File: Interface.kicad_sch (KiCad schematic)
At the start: 12 parts

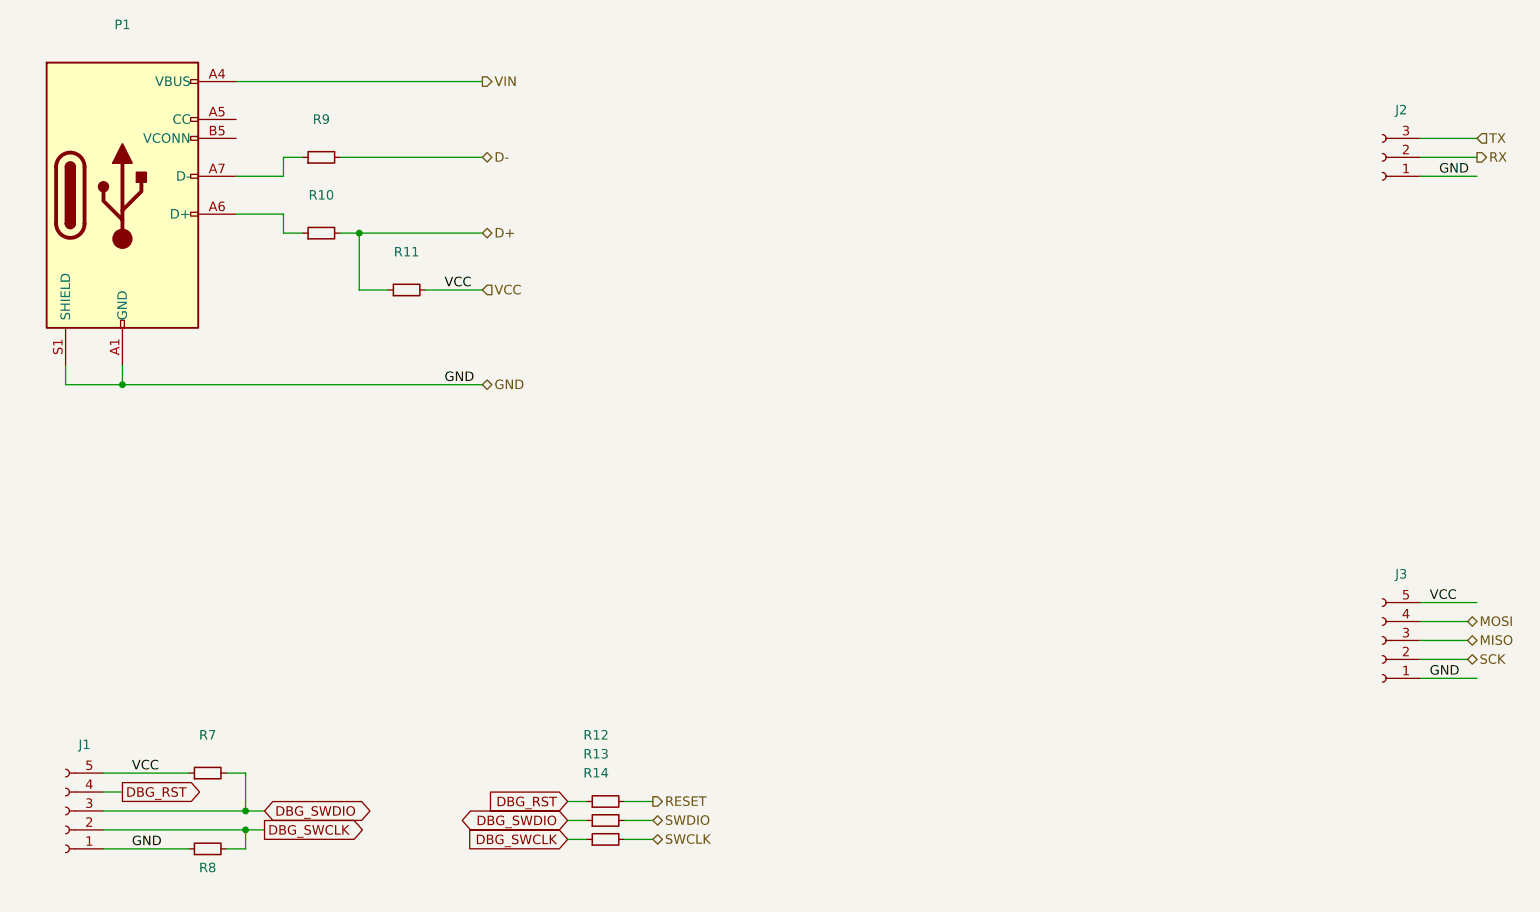
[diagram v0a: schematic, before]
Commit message: update goose60 sch footprint
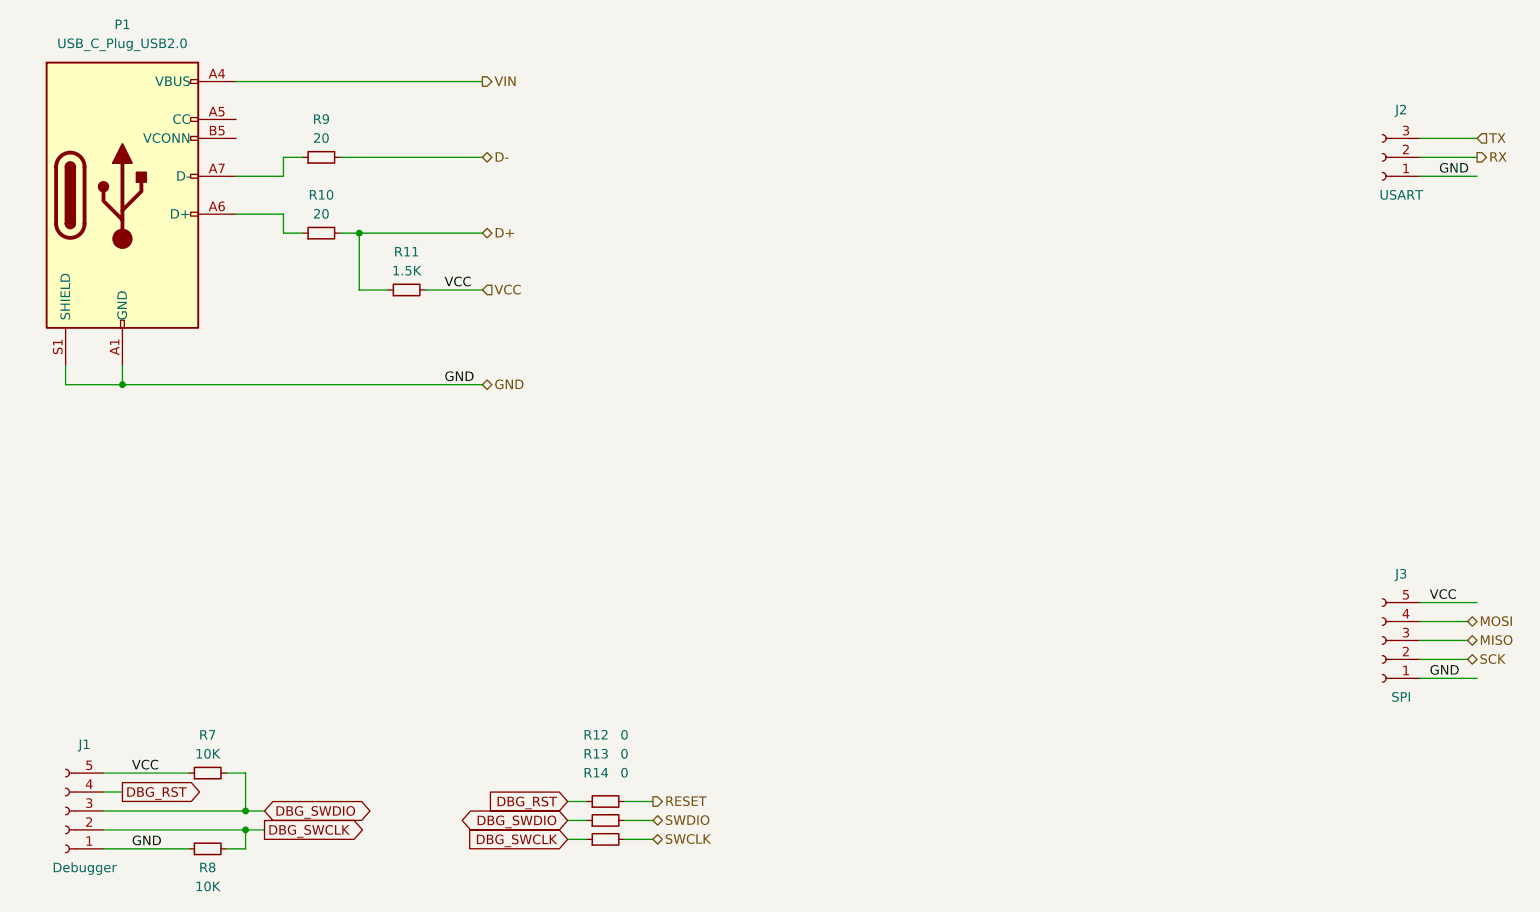
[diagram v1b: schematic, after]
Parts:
- J1: value (none) -> Debugger; footprint (none) -> Connector_PinHeader_2.00mm:PinHeader_1x05_P2.00mm_Vertical
- J2: value (none) -> USART; footprint (none) -> Connector_PinHeader_2.00mm:PinHeader_1x03_P2.00mm_Vertical
- J3: value (none) -> SPI; footprint (none) -> Connector_PinHeader_2.00mm:PinHeader_1x05_P2.00mm_Vertical
- P1: value (none) -> USB_C_Plug_USB2.0; footprint (none) -> Connector_USB:USB_C_Receptacle_HRO_TYPE-C-31-M-12
- R10, R9: value (none) -> 20; footprint (none) -> Resistor_SMD:R_0805_2012Metric
- R11: value (none) -> 1.5K; footprint (none) -> Resistor_SMD:R_0805_2012Metric
- R12, R13, R14: value (none) -> 0; footprint (none) -> Resistor_SMD:R_0805_2012Metric
- R7, R8: value (none) -> 10K; footprint (none) -> Resistor_SMD:R_0805_2012Metric
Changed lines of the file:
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@@
     (in_bom yes) (on_board yes)
     (property "Reference" "R11" (id 0) (at 93.98 60.96 90))
-    (property "Value" "" (id 1) (at 93.98 63.5 90))
-    (property "Footprint" "" (id 2) (at 93.98 66.04 0)
+    (property "Value" "1.5K" (id 1) (at 93.98 63.5 90))
+    (property "Footprint" "Resistor_SMD:R_0805_2012Metric" (id 2) (at 93.98 66.04 0)
       (effects (font (size 1.27 1.27)) hide)
     )
@@
     (in_bom yes) (on_board yes)
     (property "Reference" "R8" (id 0) (at 67.31 143.51 90))
-    (property "Value" "" (id 1) (at 67.31 146.05 90))
-    (property "Footprint" "" (id 2) (at 67.31 140.97 0)
+    (property "Value" "10K" (id 1) (at 67.31 146.05 90))
+    (property "Footprint" "Resistor_SMD:R_0805_2012Metric" (id 2) (at 67.31 140.97 0)
       (effects (font (size 1.27 1.27)) hide)
     )
@@
     (in_bom yes) (on_board yes)
     (property "Reference" "R14" (id 0) (at 119.38 130.81 90))
-    (property "Value" "" (id 1) (at 123.19 130.81 90))
-    (property "Footprint" "" (id 2) (at 120.65 139.7 0)
+    (property "Value" "0" (id 1) (at 123.19 130.81 90))
+    (property "Footprint" "Resistor_SMD:R_0805_2012Metric" (id 2) (at 120.65 139.7 0)
       (effects (font (size 1.27 1.27)) hide)
     )
@@
     (in_bom yes) (on_board yes)
     (property "Reference" "J3" (id 0) (at 227.33 104.14 0))
-    (property "Value" "" (id 1) (at 227.33 120.65 0))
-    (property "Footprint" "" (id 2) (at 224.79 113.03 0)
+    (property "Value" "SPI" (id 1) (at 227.33 120.65 0))
+    (property "Footprint" "Connector_PinHeader_2.00mm:PinHeader_1x05_P2.00mm_Vertical" (id 2) (at 224.79 113.03 0)
       (effects (font (size 1.27 1.27)) hide)
     )
@@
     (in_bom yes) (on_board yes) (fields_autoplaced)
     (property "Reference" "P1" (id 0) (at 55.88 30.48 0))
-    (property "Value" "" (id 1) (at 55.88 33.02 0))
-    (property "Footprint" "" (id 2) (at 59.69 53.34 0)
+    (property "Value" "USB_C_Plug_USB2.0" (id 1) (at 55.88 33.02 0))
+    (property "Footprint" "Connector_USB:USB_C_Receptacle_HRO_TYPE-C-31-M-12" (id 2) (at 59.69 53.34 0)
       (effects (font (size 1.27 1.27)) hide)
     )
@@
     (in_bom yes) (on_board yes)
     (property "Reference" "J1" (id 0) (at 50.8 127 0))
-    (property "Value" "" (id 1) (at 50.8 143.51 0))
-    (property "Footprint" "" (id 2) (at 48.26 135.89 0)
+    (property "Value" "Debugger" (id 1) (at 50.8 143.51 0))
+    (property "Footprint" "Connector_PinHeader_2.00mm:PinHeader_1x05_P2.00mm_Vertical" (id 2) (at 48.26 135.89 0)
       (effects (font (size 1.27 1.27)) hide)
     )
@@
     (in_bom yes) (on_board yes)
     (property "Reference" "R12" (id 0) (at 119.38 125.73 90))
-    (property "Value" "" (id 1) (at 123.19 125.73 90))
-    (property "Footprint" "" (id 2) (at 120.65 134.62 0)
+    (property "Value" "0" (id 1) (at 123.19 125.73 90))
+    (property "Footprint" "Resistor_SMD:R_0805_2012Metric" (id 2) (at 120.65 134.62 0)
       (effects (font (size 1.27 1.27)) hide)
     )
@@
     (in_bom yes) (on_board yes)
     (property "Reference" "R10" (id 0) (at 82.55 53.34 90))
-    (property "Value" "" (id 1) (at 82.55 55.88 90))
-    (property "Footprint" "" (id 2) (at 82.55 58.42 0)
+    (property "Value" "20" (id 1) (at 82.55 55.88 90))
+    (property "Footprint" "Resistor_SMD:R_0805_2012Metric" (id 2) (at 82.55 58.42 0)
       (effects (font (size 1.27 1.27)) hide)
     )
@@
     (in_bom yes) (on_board yes)
     (property "Reference" "R7" (id 0) (at 67.31 125.73 90))
-    (property "Value" "" (id 1) (at 67.31 128.27 90))
-    (property "Footprint" "" (id 2) (at 67.31 130.81 0)
+    (property "Value" "10K" (id 1) (at 67.31 128.27 90))
+    (property "Footprint" "Resistor_SMD:R_0805_2012Metric" (id 2) (at 67.31 130.81 0)
       (effects (font (size 1.27 1.27)) hide)
     )
@@
     (in_bom yes) (on_board yes)
     (property "Reference" "J2" (id 0) (at 227.33 41.91 0))
-    (property "Value" "" (id 1) (at 227.33 53.34 0))
-    (property "Footprint" "" (id 2) (at 224.79 48.26 0)
+    (property "Value" "USART" (id 1) (at 227.33 53.34 0))
+    (property "Footprint" "Connector_PinHeader_2.00mm:PinHeader_1x03_P2.00mm_Vertical" (id 2) (at 224.79 48.26 0)
       (effects (font (size 1.27 1.27)) hide)
     )
@@
     (in_bom yes) (on_board yes)
     (property "Reference" "R9" (id 0) (at 82.55 43.18 90))
-    (property "Value" "" (id 1) (at 82.55 45.72 90))
-    (property "Footprint" "" (id 2) (at 82.55 48.26 0)
+    (property "Value" "20" (id 1) (at 82.55 45.72 90))
+    (property "Footprint" "Resistor_SMD:R_0805_2012Metric" (id 2) (at 82.55 48.26 0)
       (effects (font (size 1.27 1.27)) hide)
     )
@@
     (in_bom yes) (on_board yes)
     (property "Reference" "R13" (id 0) (at 119.38 128.27 90))
-    (property "Value" "" (id 1) (at 123.19 128.27 90))
-    (property "Footprint" "" (id 2) (at 120.65 137.16 0)
+    (property "Value" "0" (id 1) (at 123.19 128.27 90))
+    (property "Footprint" "Resistor_SMD:R_0805_2012Metric" (id 2) (at 120.65 137.16 0)
       (effects (font (size 1.27 1.27)) hide)
     )

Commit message: update footpoint and add pcb layout
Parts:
- R10, R11, R9: footprint Resistor_SMD:R_0805_2012Metric -> Resistor_SMD:R_0603_1608Metric
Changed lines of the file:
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@@
     (property "Reference" "R11" (id 0) (at 93.98 60.96 90))
     (property "Value" "1.5K" (id 1) (at 93.98 63.5 90))
-    (property "Footprint" "Resistor_SMD:R_0805_2012Metric" (id 2) (at 93.98 66.04 0)
+    (property "Footprint" "Resistor_SMD:R_0603_1608Metric" (id 2) (at 93.98 66.04 0)
       (effects (font (size 1.27 1.27)) hide)
     )
@@
     (property "Reference" "R10" (id 0) (at 82.55 53.34 90))
     (property "Value" "20" (id 1) (at 82.55 55.88 90))
-    (property "Footprint" "Resistor_SMD:R_0805_2012Metric" (id 2) (at 82.55 58.42 0)
+    (property "Footprint" "Resistor_SMD:R_0603_1608Metric" (id 2) (at 82.55 58.42 0)
       (effects (font (size 1.27 1.27)) hide)
     )
@@
     (property "Reference" "R9" (id 0) (at 82.55 43.18 90))
     (property "Value" "20" (id 1) (at 82.55 45.72 90))
-    (property "Footprint" "Resistor_SMD:R_0805_2012Metric" (id 2) (at 82.55 48.26 0)
+    (property "Footprint" "Resistor_SMD:R_0603_1608Metric" (id 2) (at 82.55 48.26 0)
       (effects (font (size 1.27 1.27)) hide)
     )

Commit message: update components location
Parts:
- R12, R13, R14, R7, R8: footprint Resistor_SMD:R_0805_2012Metric -> Resistor_SMD:R_0603_1608Metric
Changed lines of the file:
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@@
     (property "Reference" "R8" (id 0) (at 67.31 143.51 90))
     (property "Value" "10K" (id 1) (at 67.31 146.05 90))
-    (property "Footprint" "Resistor_SMD:R_0805_2012Metric" (id 2) (at 67.31 140.97 0)
+    (property "Footprint" "Resistor_SMD:R_0603_1608Metric" (id 2) (at 67.31 140.97 0)
       (effects (font (size 1.27 1.27)) hide)
     )
@@
     (property "Reference" "R14" (id 0) (at 119.38 130.81 90))
     (property "Value" "0" (id 1) (at 123.19 130.81 90))
-    (property "Footprint" "Resistor_SMD:R_0805_2012Metric" (id 2) (at 120.65 139.7 0)
+    (property "Footprint" "Resistor_SMD:R_0603_1608Metric" (id 2) (at 120.65 139.7 0)
       (effects (font (size 1.27 1.27)) hide)
     )
@@
     (property "Reference" "R12" (id 0) (at 119.38 125.73 90))
     (property "Value" "0" (id 1) (at 123.19 125.73 90))
-    (property "Footprint" "Resistor_SMD:R_0805_2012Metric" (id 2) (at 120.65 134.62 0)
+    (property "Footprint" "Resistor_SMD:R_0603_1608Metric" (id 2) (at 120.65 134.62 0)
       (effects (font (size 1.27 1.27)) hide)
     )
@@
     (property "Reference" "R7" (id 0) (at 67.31 125.73 90))
     (property "Value" "10K" (id 1) (at 67.31 128.27 90))
-    (property "Footprint" "Resistor_SMD:R_0805_2012Metric" (id 2) (at 67.31 130.81 0)
+    (property "Footprint" "Resistor_SMD:R_0603_1608Metric" (id 2) (at 67.31 130.81 0)
       (effects (font (size 1.27 1.27)) hide)
     )
@@
     (property "Reference" "R13" (id 0) (at 119.38 128.27 90))
     (property "Value" "0" (id 1) (at 123.19 128.27 90))
-    (property "Footprint" "Resistor_SMD:R_0805_2012Metric" (id 2) (at 120.65 137.16 0)
+    (property "Footprint" "Resistor_SMD:R_0603_1608Metric" (id 2) (at 120.65 137.16 0)
       (effects (font (size 1.27 1.27)) hide)
     )

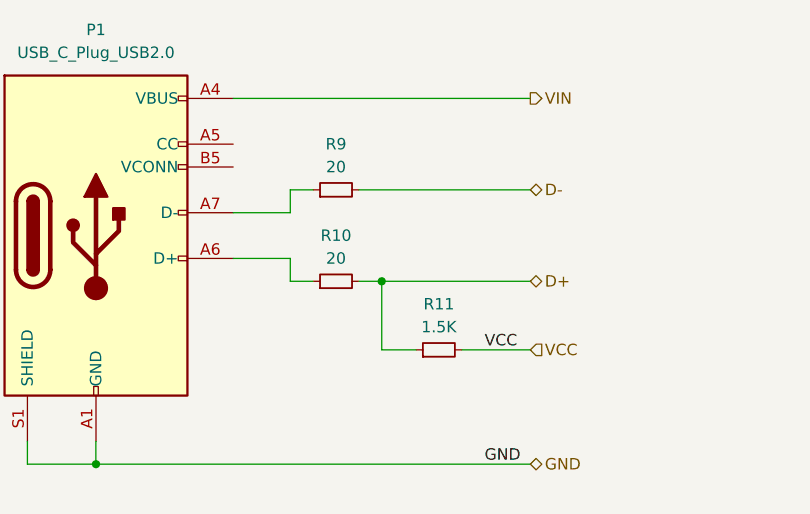
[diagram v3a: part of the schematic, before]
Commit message: add res and fix rule check fail problom
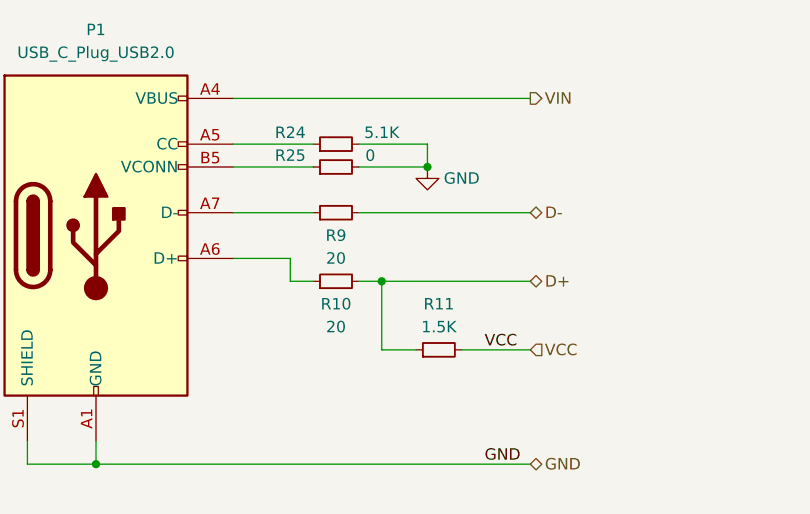
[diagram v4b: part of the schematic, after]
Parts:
- added R24: 5.1K, Resistor_SMD:R_0603_1608Metric, symbol Device:R_Small
- added R25: 0, Resistor_SMD:R_0603_1608Metric, symbol Device:R_Small
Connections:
- net GND: now also R24.2, R25.2
- net at P1.A5 (CC): now also R24.1
- net at P1.B5 (VCONN): now also R25.1
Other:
- moved on the sheet: R9
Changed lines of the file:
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@@
   (junction (at 72.39 135.89) (diameter 0) (color 0 0 0 0)
   )
+  (junction (at 92.71 45.72) (diameter 0) (color 0 0 0 0)
+  )
   (junction (at 55.88 78.74) (diameter 0) (color 0 0 0 0)
   )
   (junction (at 72.39 138.43) (diameter 0) (color 0 0 0 0)
   )
-  (wire (pts (xy 85.09 48.26) (xy 104.14 48.26))
+  (wire (pts (xy 85.09 50.8) (xy 104.14 50.8))
     (stroke (width 0) (type default) (color 0 0 0 0))
   )
@@
     (stroke (width 0) (type default) (color 0 0 0 0))
   )
+  (wire (pts (xy 92.71 43.18) (xy 92.71 45.72))
+    (stroke (width 0) (type default) (color 0 0 0 0))
+  )
   (wire (pts (xy 229.87 48.26) (xy 237.49 48.26))
     (stroke (width 0) (type default) (color 0 0 0 0))
@@
     (stroke (width 0) (type default) (color 0 0 0 0))
   )
-  (wire (pts (xy 71.12 50.8) (xy 77.47 50.8))
+  (wire (pts (xy 71.12 45.72) (xy 80.01 45.72))
     (stroke (width 0) (type default) (color 0 0 0 0))
   )
@@
     (stroke (width 0) (type default) (color 0 0 0 0))
   )
-  (wire (pts (xy 77.47 50.8) (xy 77.47 48.26))
-    (stroke (width 0) (type default) (color 0 0 0 0))
-  )
   (wire (pts (xy 53.34 133.35) (xy 55.88 133.35))
     (stroke (width 0) (type default) (color 0 0 0 0))
   )
-  (wire (pts (xy 77.47 48.26) (xy 80.01 48.26))
-    (stroke (width 0) (type default) (color 0 0 0 0))
-  )
   (wire (pts (xy 72.39 138.43) (xy 74.93 138.43))
     (stroke (width 0) (type default) (color 0 0 0 0))
@@
     (stroke (width 0) (type default) (color 0 0 0 0))
   )
+  (wire (pts (xy 85.09 43.18) (xy 92.71 43.18))
+    (stroke (width 0) (type default) (color 0 0 0 0))
+  )
   (wire (pts (xy 53.34 138.43) (xy 72.39 138.43))
     (stroke (width 0) (type default) (color 0 0 0 0))
@@
     (stroke (width 0) (type default) (color 0 0 0 0))
   )
+  (wire (pts (xy 71.12 50.8) (xy 80.01 50.8))
+    (stroke (width 0) (type default) (color 0 0 0 0))
+  )
   (wire (pts (xy 87.63 58.42) (xy 104.14 58.42))
     (stroke (width 0) (type default) (color 0 0 0 0))
   )
+  (wire (pts (xy 71.12 43.18) (xy 80.01 43.18))
+    (stroke (width 0) (type default) (color 0 0 0 0))
+  )
   (wire (pts (xy 72.39 130.81) (xy 72.39 135.89))
     (stroke (width 0) (type default) (color 0 0 0 0))
@@
   )
   (wire (pts (xy 115.57 137.16) (xy 118.11 137.16))
+    (stroke (width 0) (type default) (color 0 0 0 0))
+  )
+  (wire (pts (xy 85.09 45.72) (xy 92.71 45.72))
     (stroke (width 0) (type default) (color 0 0 0 0))
   )
@@
     (effects (font (size 1.27 1.27)) (justify left))
   )
-  (hierarchical_label "D-" (shape bidirectional) (at 104.14 48.26 0)
+  (hierarchical_label "D-" (shape bidirectional) (at 104.14 50.8 0)
     (effects (font (size 1.27 1.27)) (justify left))
   )
@@
   (hierarchical_label "MISO" (shape bidirectional) (at 236.22 113.03 0)
     (effects (font (size 1.27 1.27)) (justify left))
+  )
+  (symbol (lib_id "Device:R_Small") (at 82.55 45.72 90) (unit 1)
+    (in_bom yes) (on_board yes)
+    (property "Reference" "R25" (id 0) (at 77.47 44.45 90))
+    (property "Value" "0" (id 1) (at 86.36 44.45 90))
+    (property "Footprint" "Resistor_SMD:R_0603_1608Metric" (id 2) (at 82.55 45.72 0)
+      (effects (font (size 1.27 1.27)) hide)
+    )
+    (property "Datasheet" "~" (id 3) (at 82.55 45.72 0)
+      (effects (font (size 1.27 1.27)) hide)
+    )
+    (pin "1")
+    (pin "2")
   )
   (symbol (lib_id "Device:R_Small") (at 93.98 66.04 90) (unit 1)
@@
     (pin "4")
     (pin "5")
+  )
+  (symbol (lib_id "Device:R_Small") (at 82.55 43.18 90) (unit 1)
+    (in_bom yes) (on_board yes)
+    (property "Reference" "R24" (id 0) (at 77.47 41.91 90))
+    (property "Value" "5.1K" (id 1) (at 87.63 41.91 90))
+    (property "Footprint" "Resistor_SMD:R_0603_1608Metric" (id 2) (at 82.55 43.18 0)
+      (effects (font (size 1.27 1.27)) hide)
+    )
+    (property "Datasheet" "~" (id 3) (at 82.55 43.18 0)
+      (effects (font (size 1.27 1.27)) hide)
+    )
+    (pin "1")
+    (pin "2")
   )
   (symbol (lib_id "Connector:USB_C_Plug_USB2.0") (at 55.88 53.34 0) (unit 1)
@@
   (symbol (lib_id "Device:R_Small") (at 82.55 58.42 90) (unit 1)
     (in_bom yes) (on_board yes)
-    (property "Reference" "R10" (id 0) (at 82.55 53.34 90))
-    (property "Value" "20" (id 1) (at 82.55 55.88 90))
+    (property "Reference" "R10" (id 0) (at 82.55 60.96 90))
+    (property "Value" "20" (id 1) (at 82.55 63.5 90))
     (property "Footprint" "Resistor_SMD:R_0603_1608Metric" (id 2) (at 82.55 58.42 0)
       (effects (font (size 1.27 1.27)) hide)
@@
     (pin "3")
   )
-  (symbol (lib_id "Device:R_Small") (at 82.55 48.26 90) (unit 1)
-    (in_bom yes) (on_board yes)
-    (property "Reference" "R9" (id 0) (at 82.55 43.18 90))
-    (property "Value" "20" (id 1) (at 82.55 45.72 90))
-    (property "Footprint" "Resistor_SMD:R_0603_1608Metric" (id 2) (at 82.55 48.26 0)
-      (effects (font (size 1.27 1.27)) hide)
-    )
-    (property "Datasheet" "~" (id 3) (at 82.55 48.26 0)
-      (effects (font (size 1.27 1.27)) hide)
-    )
+  (symbol (lib_id "power:GND") (at 92.71 45.72 0) (unit 1)
+    (in_bom yes) (on_board yes)
+    (property "Reference" "#PWR023" (id 0) (at 92.71 52.07 0)
+      (effects (font (size 1.27 1.27)) hide)
+    )
+    (property "Value" "GND" (id 1) (at 96.52 46.99 0))
+    (property "Footprint" "" (id 2) (at 92.71 45.72 0)
+      (effects (font (size 1.27 1.27)) hide)
+    )
+    (property "Datasheet" "" (id 3) (at 92.71 45.72 0)
+      (effects (font (size 1.27 1.27)) hide)
+    )
+    (pin "1")
+  )
+  (symbol (lib_id "Device:R_Small") (at 82.55 50.8 90) (unit 1)
+    (in_bom yes) (on_board yes)
+    (property "Reference" "R9" (id 0) (at 82.55 53.34 90))
+    (property "Value" "20" (id 1) (at 82.55 55.88 90))
+    (property "Footprint" "Resistor_SMD:R_0603_1608Metric" (id 2) (at 82.55 50.8 0)
+      (effects (font (size 1.27 1.27)) hide)
+    )
+    (property "Datasheet" "~" (id 3) (at 82.55 50.8 0)
+      (effects (font (size 1.27 1.27)) hide)
+    )
